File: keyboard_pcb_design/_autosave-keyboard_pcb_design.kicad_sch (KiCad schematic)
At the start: 23 parts, among them J1 USB_C_Receptacle_USB2.0_14P, U1 SC09147, U2 NCP1117-3.3_SOT223, Y1 ABM8-272-T3

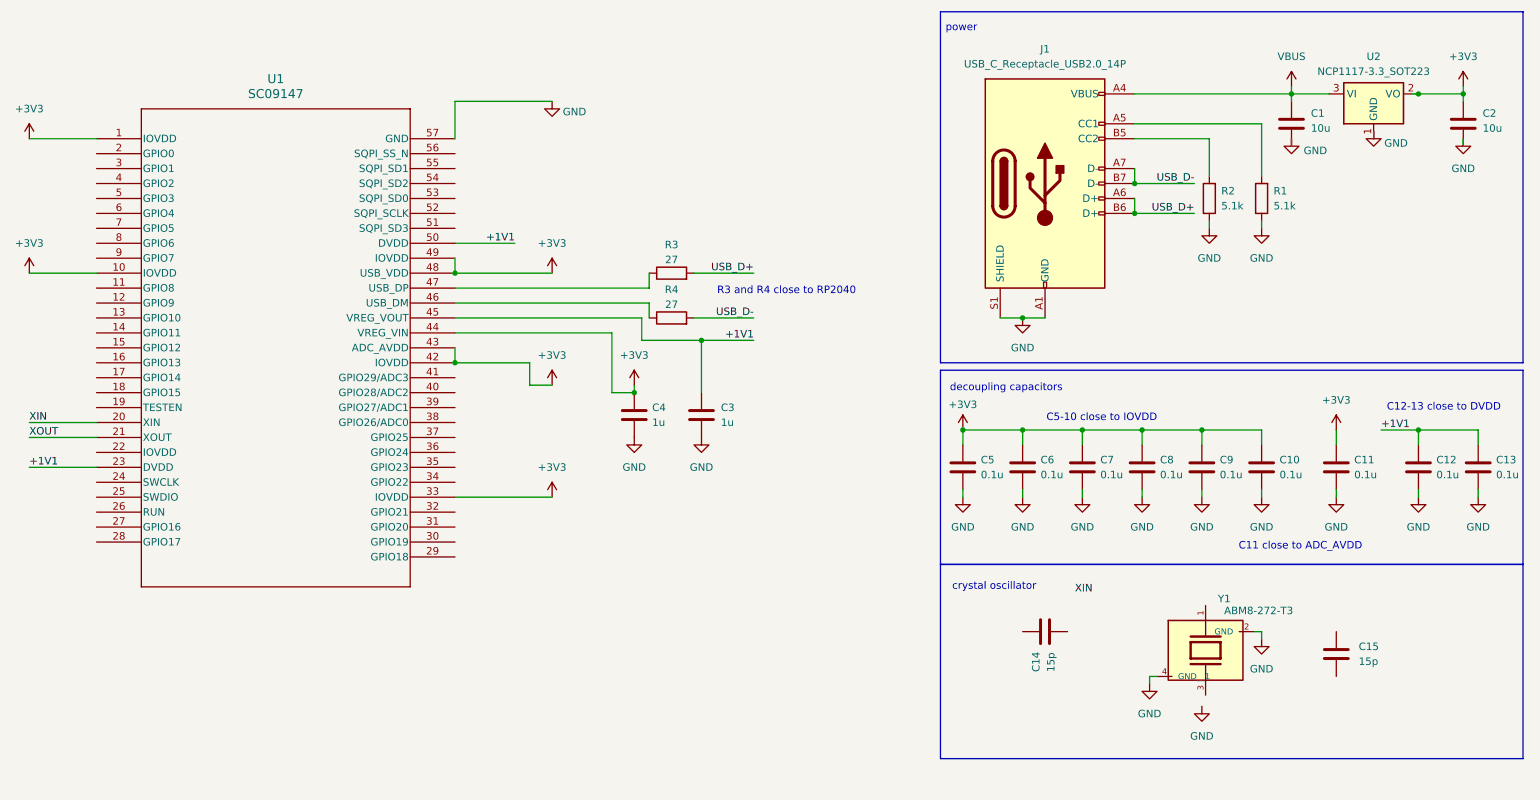
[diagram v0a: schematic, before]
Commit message: complete crystal oscillator
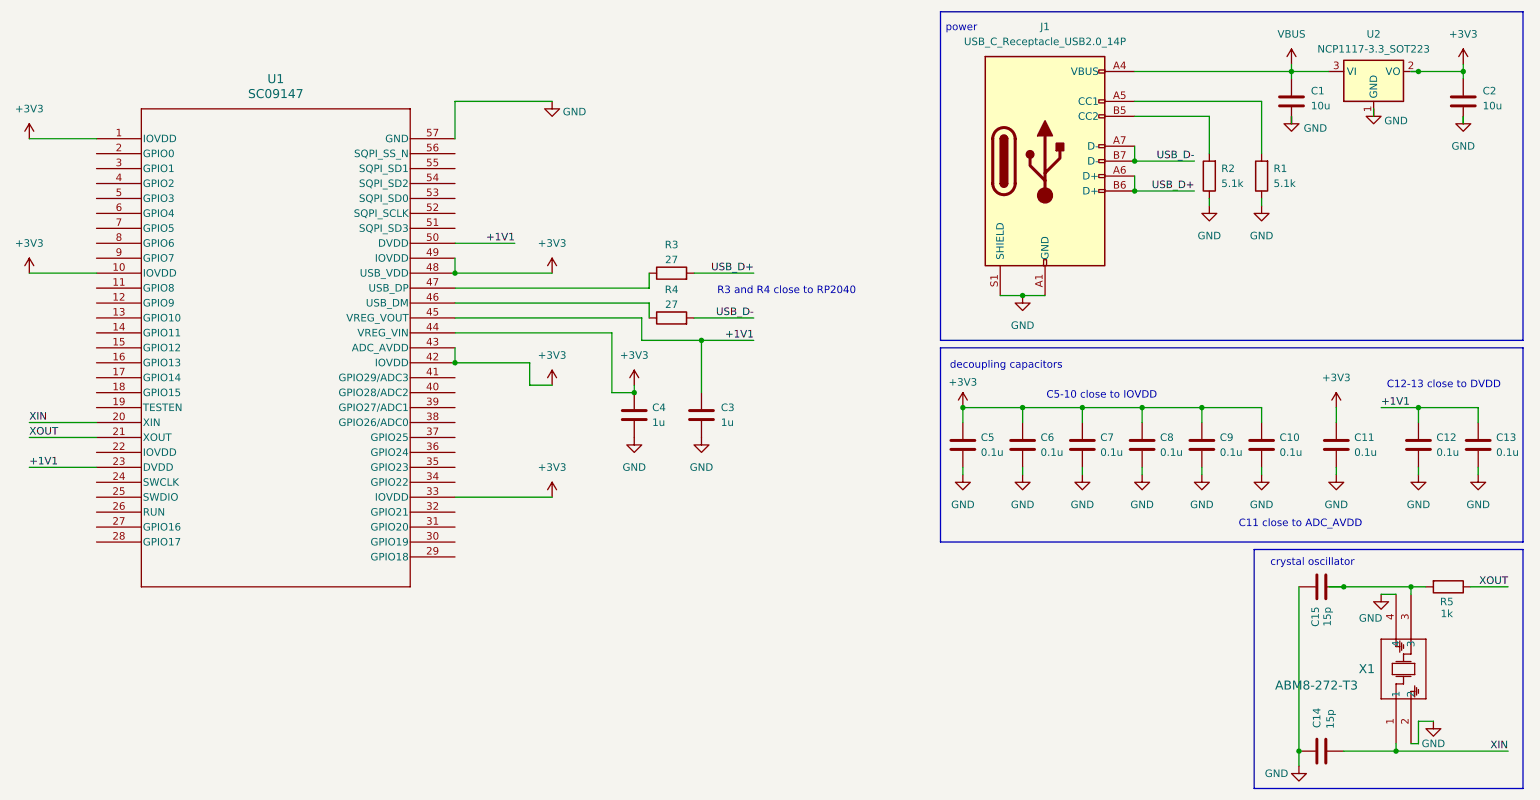
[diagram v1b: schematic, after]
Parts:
- removed Y1: ABM8-272-T3, keyboard_footprint:XTAL_ABM8-272-T3, symbol keyboard_library:ABM8-272-T3
- added R5: 1k, symbol Device:R
- added X1: ABM8-272-T3, keyboard_footprint:XTAL_ABM8-272-T3, symbol keyboard_library:ABM8-272-T3
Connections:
- net GND: now also C14.2, C15.1, X1.2, X1.4
- net XIN: now also C14.1, X1.1
- net XOUT: now also R5.1
- net at C15.2: now also R5.2, X1.3
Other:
- moved on the sheet: C1, C10, C11, C12, C13, C14, C15, C2, C5, C6, C7, C8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
